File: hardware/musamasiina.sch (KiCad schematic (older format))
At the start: 28 parts, among them P1 USB_OTG, P2 CONN_02X05, P3 CONN_02X03, P4 CONN_01X06, P5 CONN_01X03, P6 CONN_01X03, P7 CONN_01X03, SW1 SW_PUSH, U1 WT32

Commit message: Start placement of parts
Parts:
- C1, C2, C3, C5, C6, C7, C8, C9: footprint (none) -> footprints:SMD0805-CAP-M
- C4: footprint (none) -> footprints:SMD_ELEC_8mmdia-M
- D1, D2: footprint (none) -> footprints:SOD323-M
- D3: footprint (none) -> footprints:SMD0805-LED-M
- P1: footprint (none) -> Connect:USB_Micro-B_10103594-0001LF
- P2: footprint (none) -> Pin_Headers:Pin_Header_Straight_2x05_Pitch1.27mm
- P3: footprint (none) -> Pin_Headers:Pin_Header_Straight_2x03
- P4: footprint (none) -> Pin_Headers:Pin_Header_Straight_1x06
- R1, R2, R3, R4, R5, R6, R7: footprint (none) -> footprints:SMD0805-RES-M
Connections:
- net VAA: now also C7.1, C8.1
- net VESD: no longer C7.1, C8.1
- net USB_DN renamed USB_D-
- net USB_DP renamed USB_D+

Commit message: Fix #8
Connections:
- net CD-: now reaches R6.1, U1.11 (USB_D-)
- net CD+: now reaches R7.1, U1.12 (USB_D+)
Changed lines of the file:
@@
 F1 "analog.sch" 60
 F2 "MONO_OUT" O R 8300 1750 60
-F3 "P_LEFT" I L 6900 1350 60
-F4 "N_LEFT" I L 6900 1450 60
-F5 "P_RIGHT" I L 6900 1650 60
-F6 "N_RIGHT" I L 6900 1750 60
-F7 "LEFT_OUT" O R 8300 1350 60
-F8 "RIGHT_OUT" O R 8300 1450 60
-F9 "VAA" I L 6900 1150 60
-F10 "GNDA" I L 6900 2050 60
+F3 "LEFT_OUT" O R 8300 1350 60
+F4 "RIGHT_OUT" O R 8300 1450 60
+F5 "VAA" I L 6900 1150 60
+F6 "GNDA" I L 6900 2050 60
+F7 "LO_P" I L 6900 1350 60
+F8 "LO_N" I L 6900 1450 60
+F9 "RO_P" I L 6900 1650 60
+F10 "RO_N" I L 6900 1750 60
 $EndSheet
 Text Label 7150 4200 0    60   ~ 0
@@
 	8800 3550 8800 3650
 $Comp
-L VAA #PWR?
+L VAA #PWR025
 U 1 1 5742DBE5
 P 8800 2050
-F 0 "#PWR?" H 8800 1900 50  0001 C CNN
+F 0 "#PWR025" H 8800 1900 50  0001 C CNN
 F 1 "VAA" H 8800 2200 50  0000 C CNN
 F 2 "" H 8800 2050 50  0000 C CNN
@@
 $EndComp
 $Comp
-L VAA #PWR?
+L VAA #PWR026
 U 1 1 5742E9A4
 P 8800 3550
-F 0 "#PWR?" H 8800 3400 50  0001 C CNN
+F 0 "#PWR026" H 8800 3400 50  0001 C CNN
 F 1 "VAA" H 8800 3700 50  0000 C CNN
 F 2 "" H 8800 3550 50  0000 C CNN
@@
 	1    0    0    -1
 $EndComp
+Text Label 4650 5000 1    20   ~ 0
+CD-
+Text Label 4650 5100 3    20   ~ 0
+CD+
+Wire Wire Line
+	6900 2050 6650 2050
+Wire Wire Line
+	6650 2050 6650 2250
+$Comp
+L GNDA #PWR?
+U 1 1 57499599
+P 6650 2250
+F 0 "#PWR?" H 6650 2000 50  0001 C CNN
+F 1 "GNDA" H 6650 2100 50  0000 C CNN
+F 2 "" H 6650 2250 50  0000 C CNN
+F 3 "" H 6650 2250 50  0000 C CNN
+	1    6650 2250
+	1    0    0    -1
+$EndComp

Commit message: Adjust layout
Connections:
- net Power Supply/GNDBUS: now also P1.4 (ID)
- no-connect marks 13 -> 12
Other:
- note added: "Add test pad for \nalternate connections\nof ID pin"
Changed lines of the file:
@@
 F10 "BATTERY+" I L 2500 1200 60
 $EndSheet
-NoConn ~ 1150 1200
 Text Label 1500 1100 2    60   ~ 0
 USB_D+
@@
 	6650 2050 6650 2250
 $Comp
-L GNDA #PWR?
+L GNDA #PWR027
 U 1 1 57499599
 P 6650 2250
-F 0 "#PWR?" H 6650 2000 50  0001 C CNN
+F 0 "#PWR027" H 6650 2000 50  0001 C CNN
 F 1 "GNDA" H 6650 2100 50  0000 C CNN
 F 2 "" H 6650 2250 50  0000 C CNN
@@
 	1    0    0    -1
 $EndComp
+Wire Wire Line
+	1150 1200 1300 1200
+Wire Wire Line
+	1300 1200 1300 1300
+Connection ~ 1300 1300
+Text Notes 1050 1600 0    60   ~ 0
+Add test pad for \nalternate connections\nof ID pin
 $EndSCHEMATC

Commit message: Update schematics
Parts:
- C4: footprint footprints:SMD_ELEC_8mmdia-M -> footprints:C_Radial_D6.3_L13_P2-5_Bent
- P3: footprint Pin_Headers:Pin_Header_Straight_2x03 -> kicad_lib:Pin_Header_Straight_1x06
- P5, P6, P7: footprint (none) -> footprints:SMD_3-5mm_jack_CUI-SJ-352X-SMT
- SW1: value SW_PUSH -> EP11SD1SA1BE
- U1: footprint (none) -> footprints:WT32
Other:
- note added: "High output drive:\nLow current consumption:\nHigh performance:"
- note added: "TS925\nLTC6257\nOPA4322S\n"

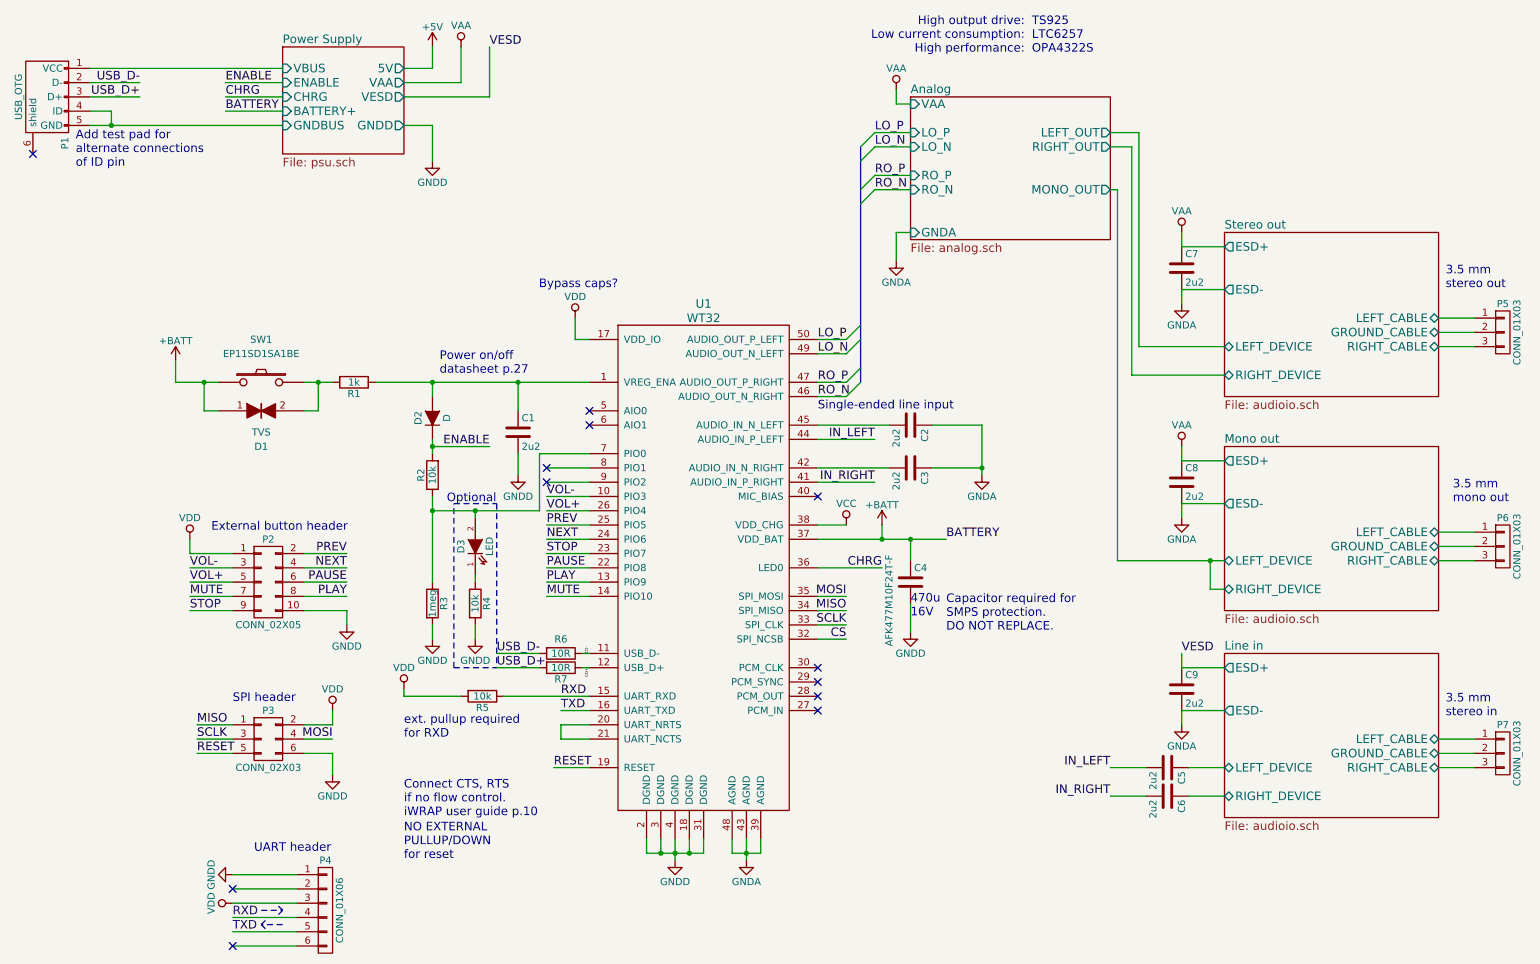
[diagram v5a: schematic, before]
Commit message: Make minimal circuitry
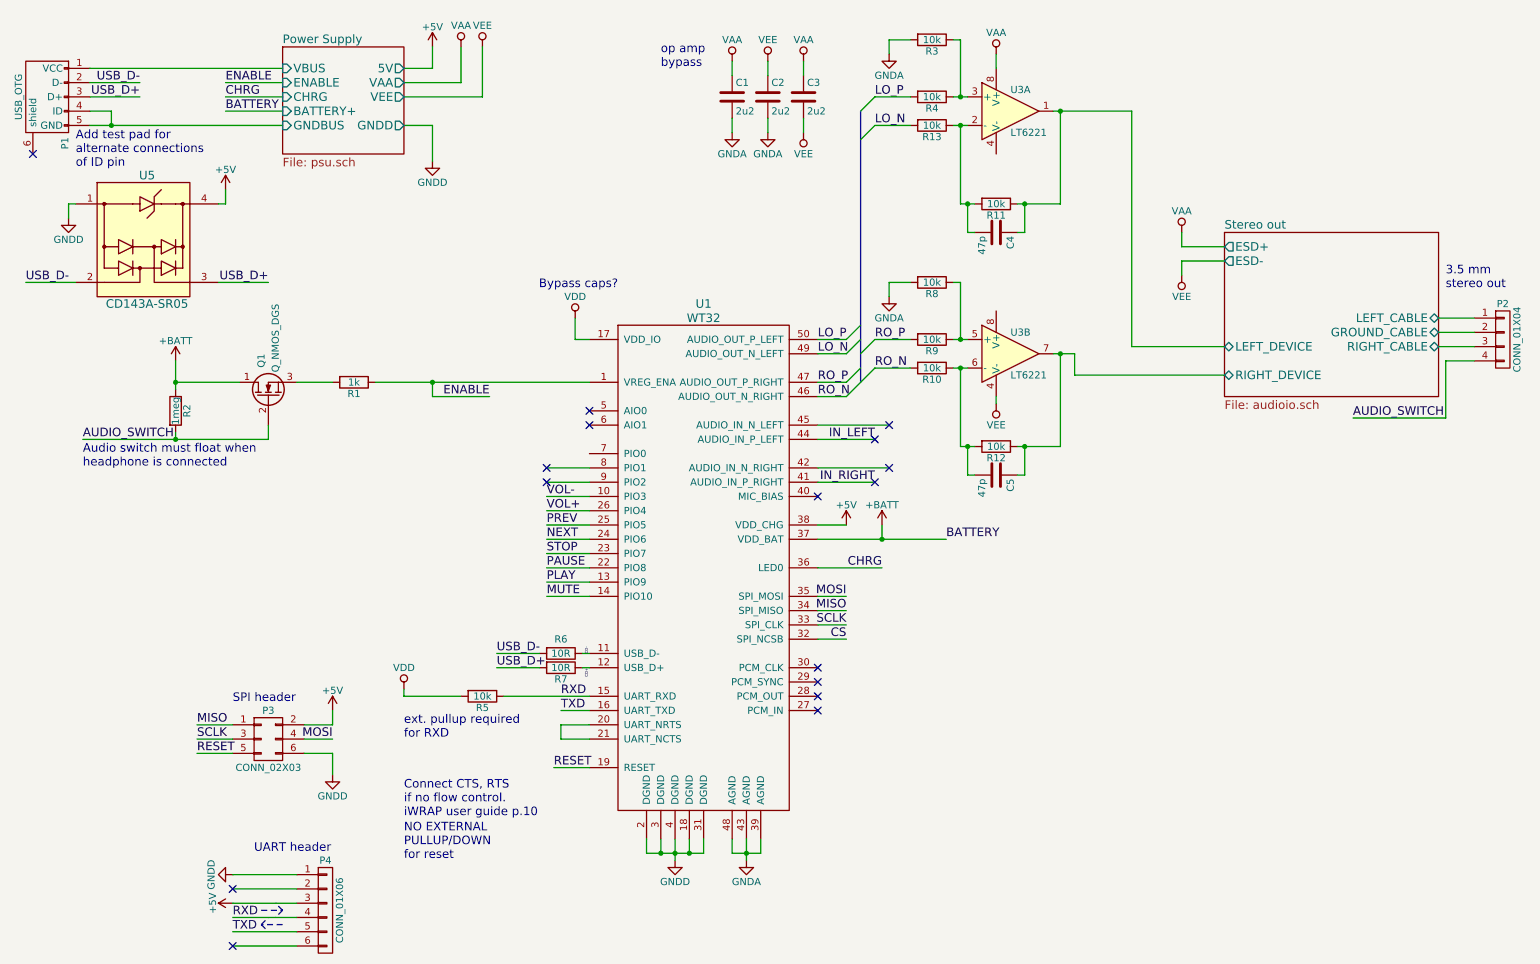
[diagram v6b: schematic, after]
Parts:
- removed C6, C7, C8, C9: 2u2, footprints:SMD0805-CAP-M, symbol C
- removed D1: TVS, footprints:SOD323-M, symbol TVS
- removed D2: D, footprints:SOD323-M, symbol D
- removed D3: LED, footprints:SMD0805-LED-M, symbol LED
- removed P2: CONN_02X05, Pin_Headers:Pin_Header_Straight_2x05_Pitch1.27mm, symbol CONN_02X05
- removed P5, P6, P7: CONN_01X03, footprints:SMD_3-5mm_jack_CUI-SJ-352X-SMT, symbol CONN_01X03
- removed SW1: EP11SD1SA1BE, symbol SW_PUSH
- added P2: CONN_01X04, footprints:SMD_3-5mm_jack_CUI-SJ-352X-SMT, symbol CONN_01X04
- added Q1: Q_NMOS_DGS, footprints:SOT23-M, symbol Q_NMOS_DGS
- added R10, R11, R12, R13, R8, R9: 10k, footprints:SMD0402-RES-N, symbol R
- added U3: LT6221, footprints:DFN-8-EP-0_5mm_3x3mm-N, symbol ADA4075
- added U5: CD143A-SR05, footprints:SOT143-N, symbol CD143A-SR05
- C1, C2, C3: footprint footprints:SMD0805-CAP-M -> footprints:SMD0402-CAP-N
- C4: value AFK477M10F24T-F -> 47p; footprint footprints:C_Radial_D6.3_L13_P2-5_Bent -> footprints:SMD0402-CAP-N
- C5: value 2u2 -> 47p; footprint footprints:SMD0805-CAP-M -> footprints:SMD0402-CAP-N
- R1, R4, R5, R6, R7: footprint footprints:SMD0805-RES-M -> footprints:SMD0402-RES-N
- R2: value 10k -> 1meg; footprint footprints:SMD0805-RES-M -> footprints:SMD0402-RES-N
- R3: value 1meg -> 10k; footprint footprints:SMD0805-RES-M -> footprints:SMD0402-RES-N
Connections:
- net VCC is gone; now on net +5V: U1.38 (VDD_CHG)
- net +5V: now also P3.2 (P2), P4.3 (P3), U5.4
- net +BATT: now also R2.1, Q1.1 (D); no longer C4.1
- net ENABLE: now also R1.1, U1.1 (VREG_ENA); no longer R2.2
- net GNDA: now also C1.2, C2.2, R3.2, R8.2; no longer C2.1, C3.1
- net GNDD: now also U5.1; no longer C1.2, C4.2, R3.2, R4.2
- net IN_LEFT: no longer C5.2
- net LO_N: now also R13.2
- net LO_P: now also R4.2
- net RO_N: now also R10.2
- net RO_P: now also R9.2
- net Stereo out/GROUND_CABLE: now also P2.2 (P2)
- net Stereo out/LEFT_CABLE: now also P2.1 (P1)
- net Stereo out/RIGHT_CABLE: now also P2.3 (P3)
- net USB_D+: now also U5.3
- net USB_D-: now also U5.2
- net VAA: now also C1.1, C3.1, U3.8 (V+)
- net VDD: no longer P3.2 (P2), P4.3 (P3)
- net at U1.42 (AUDIO_IN_N_RIGHT): no longer C3.2
- net at U1.45 (AUDIO_IN_N_LEFT): no longer C2.2
- net at R1.2: now also Q1.3 (S)
- net at R4.1: now also R3.1, U3.3 (+)
- net Line in/LEFT_DEVICE renamed Stereo out/RIGHT_DEVICE
- net Stereo out/RIGHT_DEVICE: now also R12.1, U3.7
- new net: C4.2, R11.2, R13.1, U3.2 (-)
- new net: R8.1, R9.1, U3.5 (+)
- new net: C5.2, R10.1, R12.2, U3.6 (-)
- new net AUDIO_SWITCH: P2.4 (P4), Q1.2 (G), R2.2
- new net Stereo out/LEFT_DEVICE: C4.1, R11.1, U3.1
- new net VEE: C2.1, C3.2, U3.4 (V-)
- now unconnected: U1.7 (PIO0)
- no-connect marks 12 -> 16
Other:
- note added: "Audio switch must float when \nheadphone is connected"
- note added: "op amp\nbypass"
- note removed: "3.5 mm\nmono out"
- note removed: "3.5 mm\nstereo in"
- note removed: "470u\n16V"
- note removed: "Capacitor required for \nSMPS protection.\nDO NOT REPLACE."
- note removed: "External button header"
- note removed: "High output drive:\nLow current consumption:\nHigh performance:"
- note removed: "Optional"
- note removed: "Power on/off\ndatasheet p.27"
- note removed: "Single-ended line input"
- note removed: "TS925\nLTC6257\nOPA4322S\n"

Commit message: Finalize design
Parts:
- added C8: 2u2, footprints:SMD0402-CAP-N, symbol C
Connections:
- net +BATT: now also C8.1
- net CS: now also P4.2 (P2)
- net GNDD: now also C8.2
- no-connect marks 16 -> 15
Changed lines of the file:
@@
 F9 "BATTERY+" I L 2500 1200 60
 F10 "VEE" O R 3350 1100 60
+F11 "VDD" O R 3350 1200 60
 $EndSheet
 Text Label 1500 1100 2    60   ~ 0
@@
 UART header
 NoConn ~ 2150 7050
-NoConn ~ 2150 6650
 $Comp
 L GNDD #PWR011
@@
 	-1   0    0    1
 $EndComp
+Wire Wire Line
+	3350 1200 4050 1200
+Wire Wire Line
+	4050 1200 4050 750
+$Comp
+L VDD #PWR030
+U 1 1 5754268A
+P 4050 750
+F 0 "#PWR030" H 4050 600 50  0001 C CNN
+F 1 "VDD" H 4050 900 50  0000 C CNN
+F 2 "" H 4050 750 50  0000 C CNN
+F 3 "" H 4050 750 50  0000 C CNN
+	1    4050 750
+	1    0    0    -1
+$EndComp
+$Comp
+L C C8
+U 1 1 575433CE
+P 6850 4450
+F 0 "C8" H 6875 4550 50  0000 L CNN
+F 1 "2u2" H 6875 4350 50  0000 L CNN
+F 2 "footprints:SMD0402-CAP-N" H 6888 4300 50  0001 C CNN
+F 3 "" H 6850 4450 50  0000 C CNN
+	1    6850 4450
+	1    0    0    -1
+$EndComp
+Wire Wire Line
+	6850 4300 6850 4200
+Connection ~ 6850 4200
+Wire Wire Line
+	6850 4650 6850 4600
+$Comp
+L GNDD #PWR031
+U 1 1 57543DDC
+P 6850 4650
+F 0 "#PWR031" H 6850 4400 50  0001 C CNN
+F 1 "GNDD" H 6850 4500 50  0000 C CNN
+F 2 "" H 6850 4650 50  0000 C CNN
+F 3 "" H 6850 4650 50  0000 C CNN
+	1    6850 4650
+	1    0    0    -1
+$EndComp
+Text Label 2150 6650 0    60   ~ 0
+CS
 $EndSCHEMATC
